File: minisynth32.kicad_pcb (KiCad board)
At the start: 2 copper layers, 49.5 x 97.8 mm, 22 parts, among them J1 F_PANEL, J2 Conn_02x20_Odd_Even, J3 PJ-002A, J4 ROT_HDR, J5 MIDI_IN, J6 R_BREAKOUT, J7 SSD1306 OLED, SW1 B1, SW2 PB400EEQR1BLK, SW3 B2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

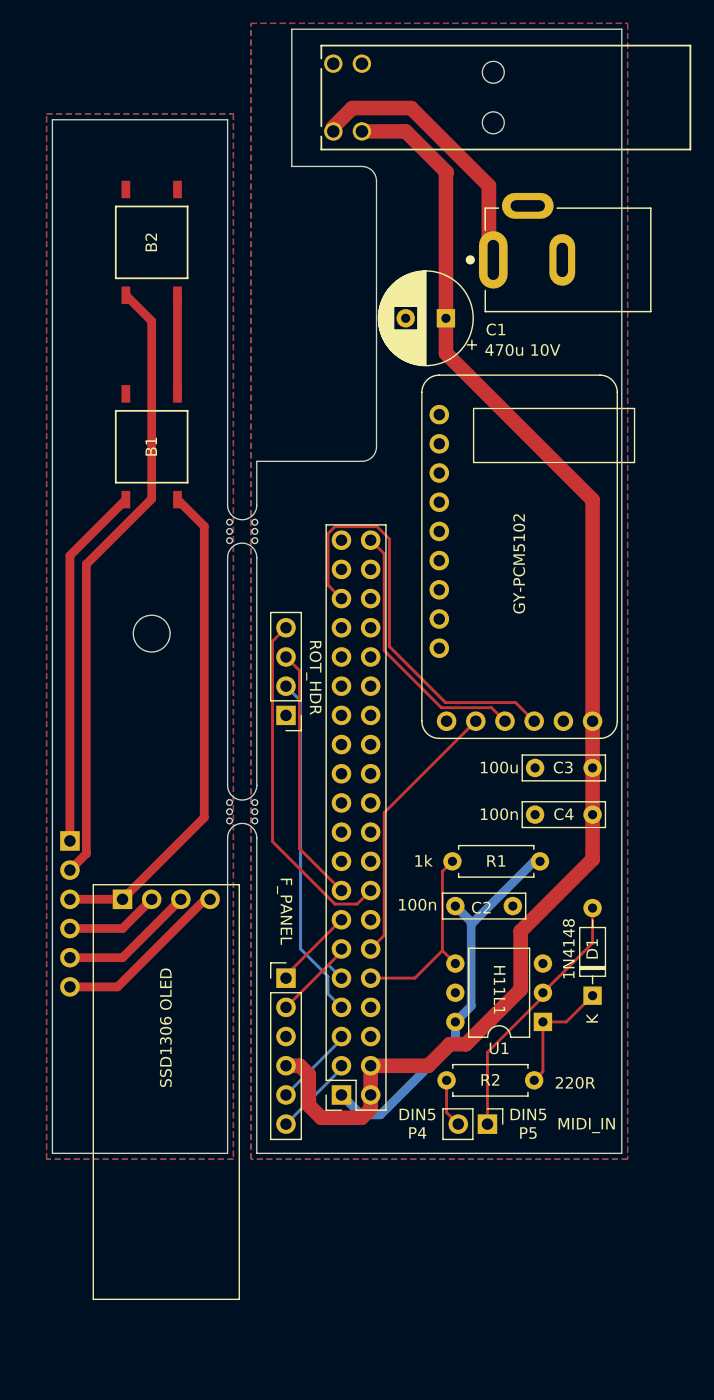
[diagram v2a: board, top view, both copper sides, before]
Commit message: Rev 1.1 F/R PCBs, tuned base and top
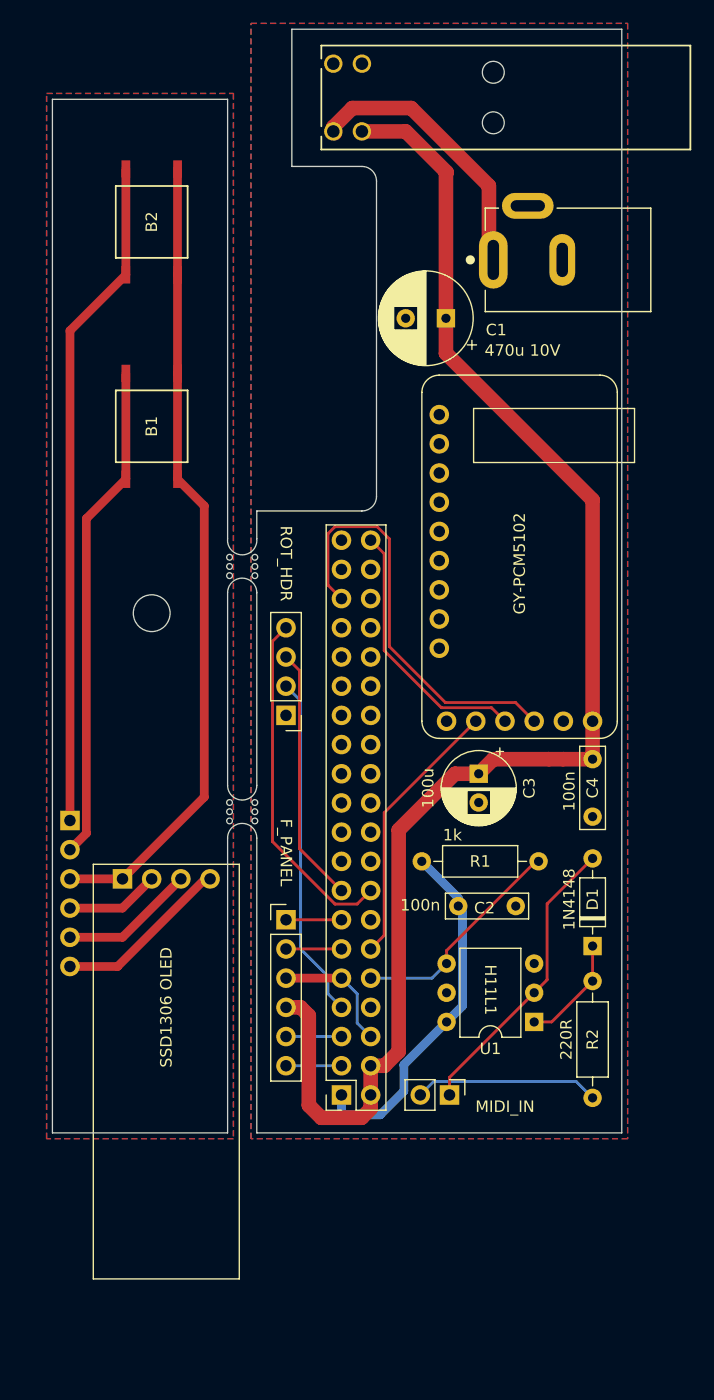
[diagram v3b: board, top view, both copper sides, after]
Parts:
- C3: footprint Capacitor_THT:C_Rect_L7.0mm_W2.0mm_P5.00mm -> Capacitor_THT:CP_Radial_D6.3mm_P2.50mm
- R1, R2: footprint Resistor_THT:R_Axial_DIN0207_L6.3mm_D2.5mm_P7.62mm_Horizontal -> Resistor_THT:R_Axial_DIN0207_L6.3mm_D2.5mm_P10.16mm_Horizontal
- moved R2 12.8 mm to (158.8, 136.9), turned to 90 degrees
- moved C3 9.92 mm to (148.8, 108.7), turned to 270 degrees
- moved R1 7.49 mm to (154.1, 116.3), turned to 180 degrees
- moved J1 5.08 mm to (132.1, 121.4)
- moved C4 4.83 mm to (158.8, 107.4), turned to 270 degrees
- moved D1 4.32 mm to (158.8, 123.7)
- moved J5 4.17 mm to (146.3, 136.7)
- moved mouse-bite-2.54mm-slot 3.05 mm to (128.3, 90.7)
- moved J6 1.78 mm to (113.3, 112.8)
- moved SW3 1.78 mm to (120.4, 60.7)
- moved J7 1.78 mm to (121.7, 134.6)
- moved REF** 1.78 mm to (120.4, 94.7)
- moved SW1 1.78 mm to (120.4, 78.5)
- moved U1 0.76 mm to (153.7, 130.3)
- moved C2 0.25 mm to (147.1, 120.2)
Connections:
- SW1 pad 2: Net-(SW1-Pad2) -> Net-(J6-Pad3)
- SW1 pad 3: Net-(J6-Pad1) -> Net-(J6-Pad2)
- SW1 pad 4: Net-(SW1-Pad4) -> Net-(J6-Pad2)
- SW3 pad 1: Net-(SW1-Pad2) -> Net-(J6-Pad3)
- SW3 pad 2: Net-(SW3-Pad2) -> Net-(J6-Pad3)
- SW3 pad 3: Net-(J6-Pad2) -> Net-(J6-Pad1)
- SW3 pad 4: Net-(SW3-Pad4) -> Net-(J6-Pad1)
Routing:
- net Net-(J6-Pad3): track 43.3 -> 70.2 mm
- net Net-(J6-Pad1): track 31.7 -> 58.7 mm
- net Net-(J5-Pad2): track 4.23 -> 16.1 mm
- net Net-(J6-Pad2): track 53.9 -> 43.4 mm
- net GND: track 1.44 -> 11.0 mm
- net Net-(SW1-Pad2): track 8.59 -> 0.00 mm
- net +5V: track 118.7 -> 126.8 mm
- net Net-(D1-Pad2): track 22.6 -> 25.7 mm
- net +3V3: track 34.3 -> 31.5 mm
- net /GPIO15(RXD0): track 16.9 -> 19.5 mm
- net BTN2: track 7.08 -> 4.83 mm
- net BTN1: track 7.08 -> 5.08 mm
- net I2C_SCL: track 7.08 -> 5.08 mm
- net I2C_SDA: track 7.08 -> 5.33 mm
- net Net-(D1-Pad1): track 10.7 -> 9.60 mm
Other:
- board size 49.5 x 97.8 mm -> 49.5 x 96 mm
- board text added: "F_PANEL"
- board text added: "MIDI_IN"
- board text added: "Minisynth 32: Front panel board https://github.com/grantek/minisynth32 Rev 1.1"
- board text added: "Minisynth 32: Rear panel breakout board https://github.com/grantek/minisynth32 Rev 1.1"
- board text added: "P4"
- board text added: "ROT_HDR"
- board text added: "SDA SCL VCC GND B1 B2"
- board text removed: "DIN5 P4"
- board text removed: "Minisynth 32: Front panel board https://github.com/grantek/minisynth32"
- board text removed: "Minisynth 32: Rear panel breakout board https://github.com/grantek/minisynth32"
- board text removed: "SDA SCL"
- board text removed: "VCC GND B1 B2"

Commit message: front pcb v2
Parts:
- added J8: UNUSED_2, minisynth32:PinHeader_1x04_P2.54mm_Vertical, B.Cu at (123.6, 114.8)
- added J9: UNUSED_1, minisynth32:PinHeader_1x04_P2.54mm_Vertical, B.Cu at (118.5, 114.8)
- added SW10: SW_Push, minisynth32:TL59N, F.Cu at (122.0, 79.8)
- added SW2: B2, minisynth32:TL59N, F.Cu at (122.0, 67.8)
- added SW4: SW_Push, minisynth32:TL59N, F.Cu at (122.0, 53.8)
- added SW5: SW_Push, minisynth32:TL59N, F.Cu at (115.0, 95.8)
- added SW6: SW_Push, minisynth32:TL59N, F.Cu at (115.0, 87.8)
- added SW7: SW_Push, minisynth32:TL59N, F.Cu at (115.0, 79.8)
- added SW8: SW_Push, minisynth32:TL59N, F.Cu at (122.0, 95.8)
- added SW9: SW_Push, minisynth32:TL59N, F.Cu at (122.0, 87.8)
- SW1: footprint minisynth32:TL3301AF160QG-nopaste -> minisynth32:TL59N
- SW3: value B2 -> SW_Push; footprint minisynth32:TL3301AF160QG-nopaste -> minisynth32:TL59N
- moved REF** 14.7 mm to (118.5, 109.3)
- moved SW1 12.0 mm to (115.0, 67.8), turned to 0 degrees
- moved J6 8.86 mm to (111.6, 121.5)
- moved SW3 8.76 mm to (115.0, 53.8), turned to 0 degrees
- moved J7 8.68 mm to (119.8, 143.1)
- renumbered SW2 to SW11
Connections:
- J6 pad 3: Net-(J6-Pad3) -> GND2
- J7 pad 1: Net-(J6-Pad3) -> GND2
- SW1 pad 1: Net-(J6-Pad3) -> Net-(J6-Pad1)
- SW1 pad 2: Net-(J6-Pad3) -> GND2
- SW3 pad 1: Net-(J6-Pad3) -> Net-(J9-Pad4)
- SW3 pad 2: Net-(J6-Pad3) -> GND2
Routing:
- net Net-(J9-Pad4): track 0.00 -> 76.7 mm
- net Net-(J6-Pad3): track 70.2 -> 0.00 mm
- net Net-(J8-Pad4): track 0.00 -> 69.7 mm
- net Net-(J9-Pad3): track 0.00 -> 43.1 mm
- net Net-(J8-Pad3): track 0.00 -> 41.8 mm
- net Net-(J9-Pad2): track 0.00 -> 32.0 mm
- net Net-(J8-Pad2): track 0.00 -> 29.4 mm
- net Net-(J8-Pad1): track 0.00 -> 19.8 mm
- net Net-(J9-Pad1): track 0.00 -> 18.2 mm
- net Net-(J6-Pad2): track 43.4 -> 60.2 mm
- net Net-(J6-Pad1): track 58.7 -> 53.2 mm
- added copper zone on B.Cu, net GND2
- removed copper zone on B.Cu, net (none)
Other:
- board size 49.5 x 96 mm -> 51.3 x 96.2 mm
- board text added: "B2 B1"
- board text added: "Minisynth 32: Front panel board Rev 2.0 https://github.com/grantek/minisynth32"
- board text added: "Minisynth 32: Rear panel breakout board https://github.com/grantek/minisynth32 Rev 1.1-1.2"
- board text added: "UNUSED"
- board text added: "UNUSED: For future expansion or fake clickable buttons."
- board text removed: "B1 B2"
- board text removed: "Minisynth 32: Front panel board https://github.com/grantek/minisynth32 Rev 1.1"
- board text removed: "Minisynth 32: Rear panel breakout board https://github.com/grantek/minisynth32 Rev 1.1"

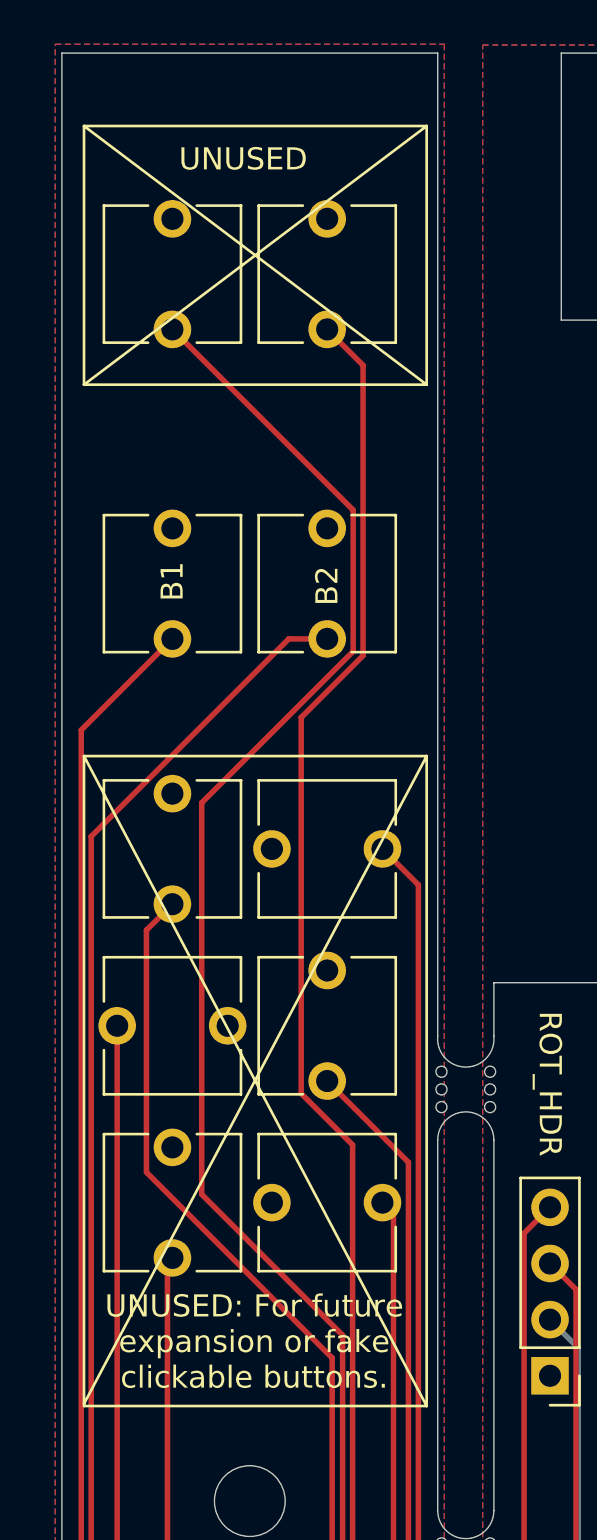
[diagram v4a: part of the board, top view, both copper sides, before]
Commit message: Silkscreen update to front and F/R PCBs
Updated Silkscreen text for extra buttons to read "NOT FUNCTIONAL" instead of "UNUSED", and got rid of the cross through them to avoid confusion.
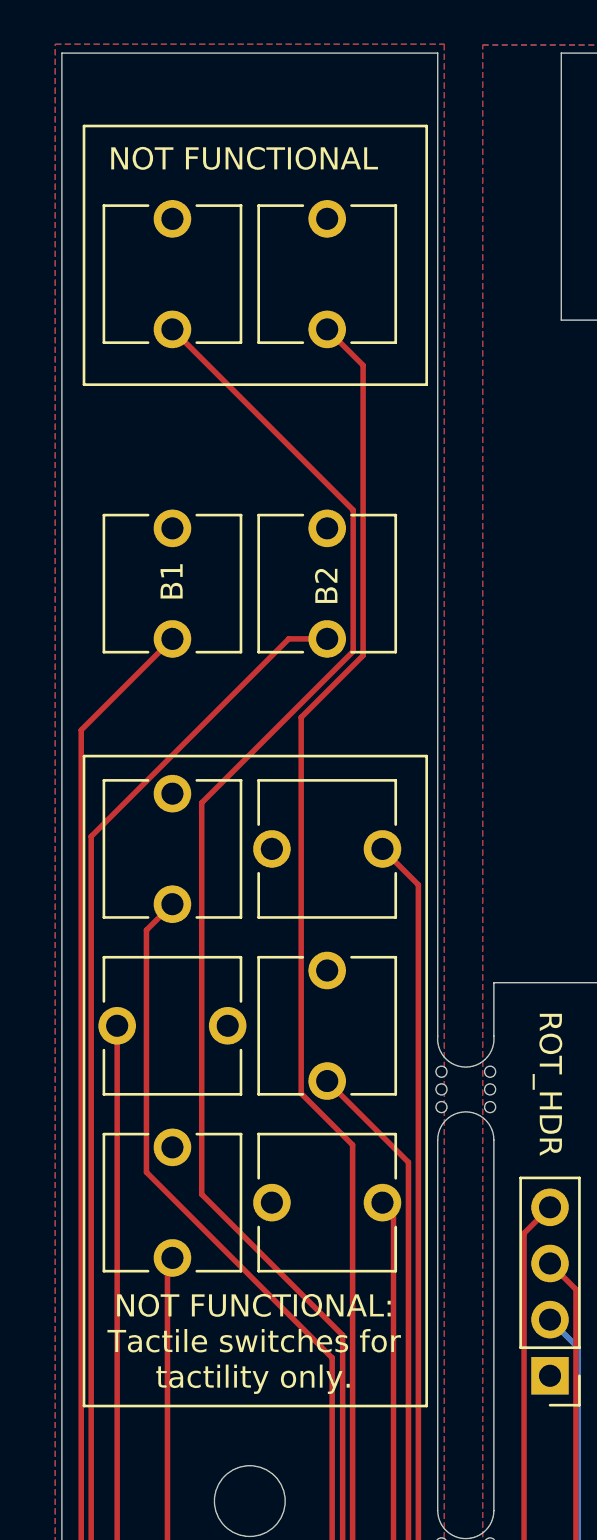
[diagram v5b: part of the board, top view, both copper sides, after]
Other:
- board text added: "NOT FUNCTIONAL"
- board text added: "NOT FUNCTIONAL: Tactile switches for tactility only."
- board text removed: "UNUSED"
- board text removed: "UNUSED: For future expansion or fake clickable buttons."
